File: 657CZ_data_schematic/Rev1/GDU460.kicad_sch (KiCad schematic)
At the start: 3 parts, among them P4X01 DE9_Socket, P4X02 DB50_Socket, P4X03 DE9_Socket

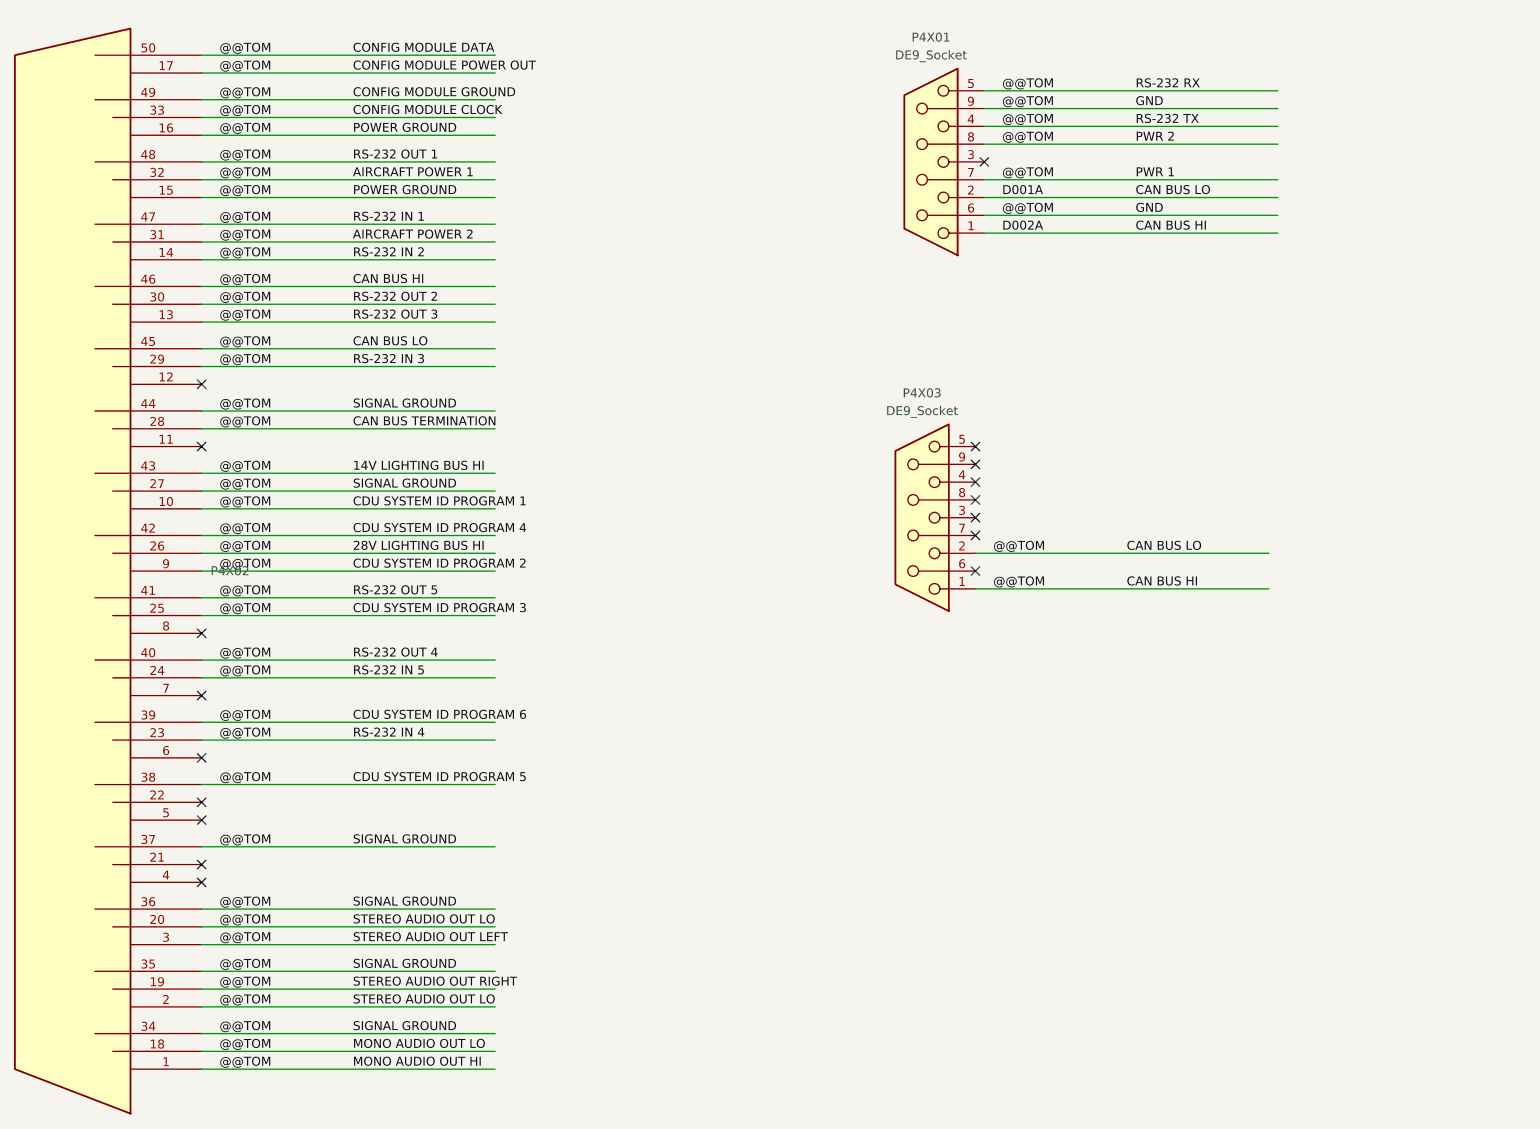
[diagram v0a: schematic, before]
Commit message: added data connections after AvClassics wiring. completed LRUs GMU, GDU, GSU, GAD, GNC, GTX, GTR  Not completed GMA, GEA and autopilot LRUs
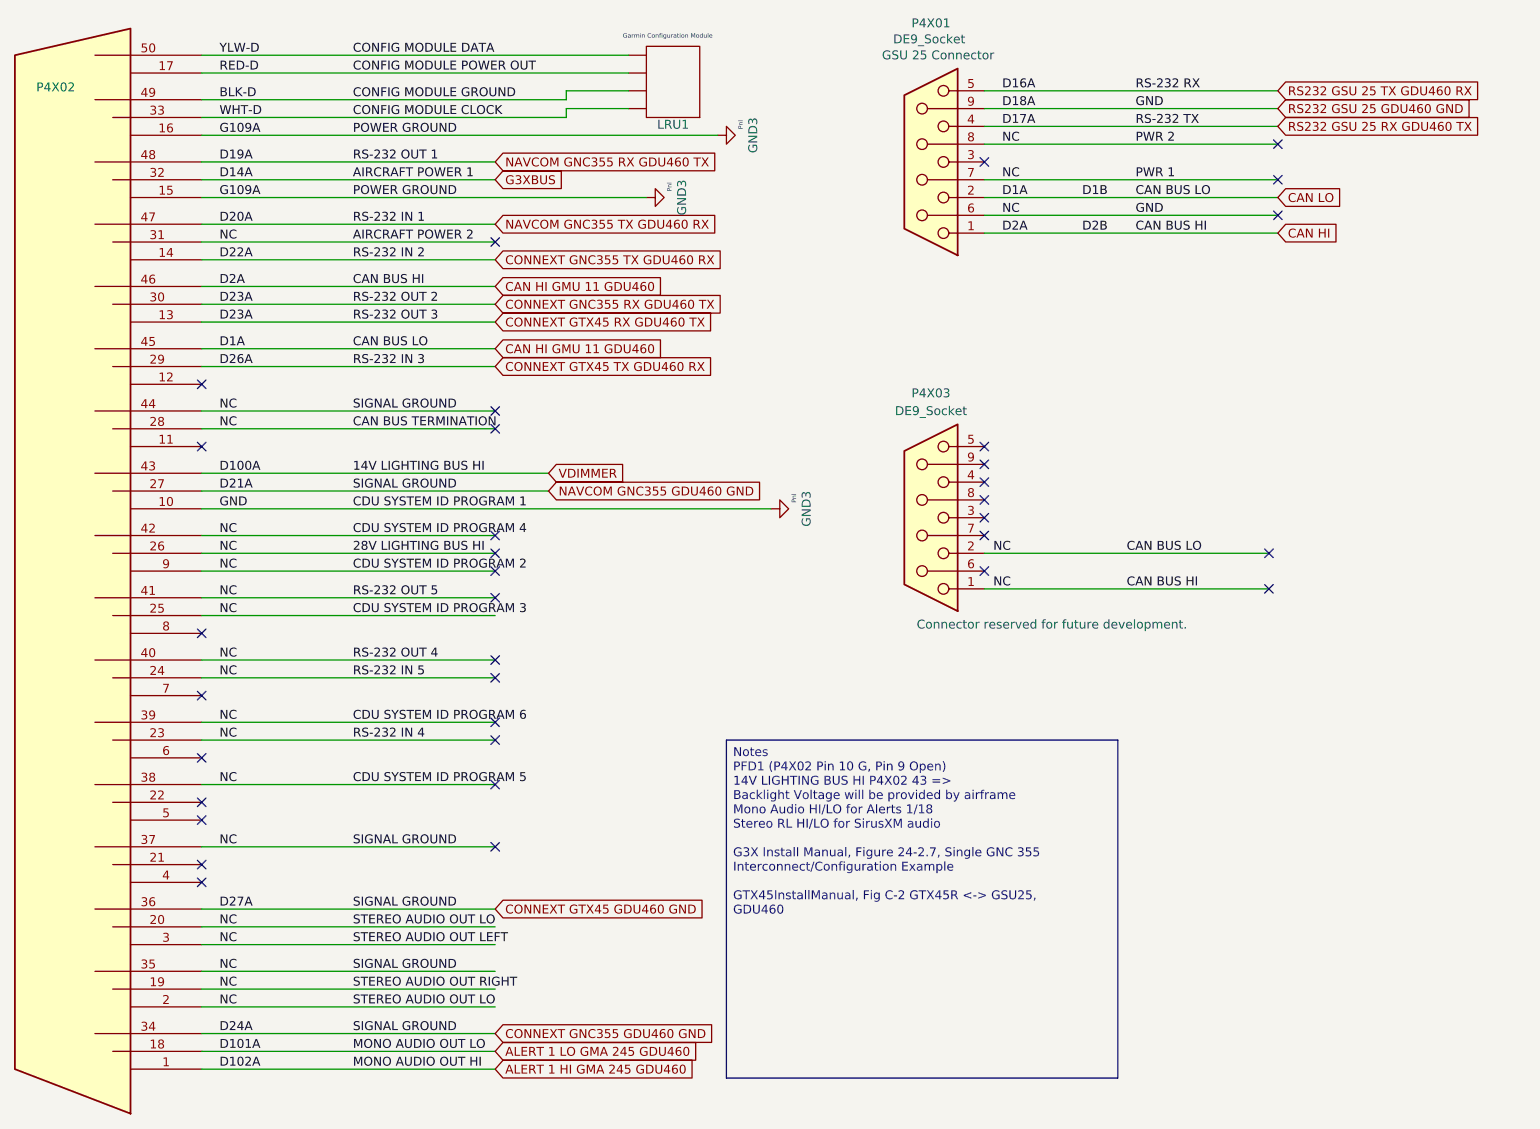
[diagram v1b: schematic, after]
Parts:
- added LRU1: ~, symbol AeroElectricConnectionSymbols:LRU_4x
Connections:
- net 14V LIGHTING BUS HI renamed GND3
- net GND3: no longer P4X01.4, P4X01.5
- new net BLK-D: LRU1.3 (Ylw)
- new net CONFIG MODULE CLOCK: LRU1.4 (Blu)
- new net CONFIG MODULE DATA: LRU1.1 (Red)
- new net CONFIG MODULE POWER OUT: LRU1.2 (Blk)
- new net RS232 GSU 25 RX GDU460 TX: P4X01.4
- new net RS232 GSU 25 TX GDU460 RX: P4X01.5
- no-connect marks 17 -> 35
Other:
- moved on the sheet: P4X03
